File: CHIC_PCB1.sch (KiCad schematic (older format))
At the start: 39 parts, among them J1 Conn_01x06_Female, P1 USB_C_Plug_USB2.0, SW1 SW_Push, U1 ATmega328P-MMH, U2 MCP73831-2-OT, U3 ESP-12E, U4 AT42QT1010-M

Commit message: Second version finished, to be verified
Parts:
- removed C7: 0.1u, Capacitor_SMD:C_0805_2012Metric, symbol Device:C
- removed C8: C, Capacitor_SMD:C_0805_2012Metric, symbol Device:C
- removed J1: Conn_01x06_Female, Connector_Harwin:Harwin_M20-89006xx_1x06_P2.54mm_Horizontal, symbol Connector:Conn_01x06_Female
- removed TP1, TP2, TP3: TestPoint, Connector_PinHeader_1.00mm:PinHeader_1x01_P1.00mm_Horizontal, symbol Connector:TestPoint
- removed U1: ATmega328P-MMH, Package_DFN_QFN:QFN-28-1EP_4x4mm_P0.45mm_EP2.4x2.4mm, symbol MCU_Microchip_ATmega:ATmega328P-MMH
- added D3: LED, symbol Device:LED
- added D4, D5: D_Schottky, symbol Device:D_Schottky
- added J1: FTDI or UART cable, symbol Connector_Generic:Conn_01x06
- added R11: 10k, symbol Device:R
- added SW2: SW_Push, symbol Switch:SW_Push
- added U1: AP2112K-3.3, Package_TO_SOT_SMD:SOT-23-5, symbol Regulator_Linear:AP2112K-3.3
- C3: value 100n -> 10u; footprint Capacitor_SMD:C_0805_2012Metric -> (none)
- R5, R9: footprint Resistor_SMD:R_0603_1608Metric -> (none)
- R6: value 10k -> 2k; footprint Resistor_SMD:R_0603_1608Metric -> (none)
- R7: value R -> 10k; footprint Resistor_SMD:R_0603_1608Metric -> (none)
- SW1: footprint Button_Switch_SMD:SW_Push_1P1T_NO_CK_KSC7xxJ -> (none)
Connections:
- net labels added: ADC, CH_PD, GPIO0, GPIO2, RXD, TXD, Vbat, Vin, nRESET
- net labels removed: MC_RX, MC_TX, VCC, Vtouch, cts, rst, ucc
- wire segments 109 -> 87
- no-connect marks 0 -> 1
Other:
- note added: "3.3V out, 500mA regulator to combine the battery input and the UART cable input.\nTherefore, it's not a problem to use 5v instead of 3.3v for the UART cable"
- note added: "Battery Charger with USB-C connection"
- note added: "CHIC Sensor Module"
- note added: "ESP8266 Module\nActs as the MC of the boad to read the sensor value and send it to host server."
- note added: "Reboot mode: "If GPIO0 is held low during power-up, it starts boot-mode".\nGPIO2 can also be used for boatload, so keep it high.\n"
- note added: "Touch Sensor Module (hopefully we can create our own soon)"
- note added: "UART Cable to flash the ESP8266, and for debuging. \nESP8266 can be flashed easily with Atom's Platform IO software."
- note removed: "Battery Charger and USB-C connection"
- note removed: "ESP8266 Wifi Module"
- note removed: "Microcontrolleur ATMega \n"
- note removed: "Touch Sensor Module"
- moved on the sheet: BatteryConnector1, C1, C2, C4, C5, C6, D1, D2, Electrode1, H1, H3, H4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

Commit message: Test de github
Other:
- note added: "fgdhgfd"
- note added: "test"
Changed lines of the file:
@@
 5v
 NoConn ~ 6950 3450
+Text Notes 450  -300 0    50   ~ 0
+test
+Text Notes 1050 -150 0    50   ~ 0
+fgdhgfd
 $EndSCHEMATC

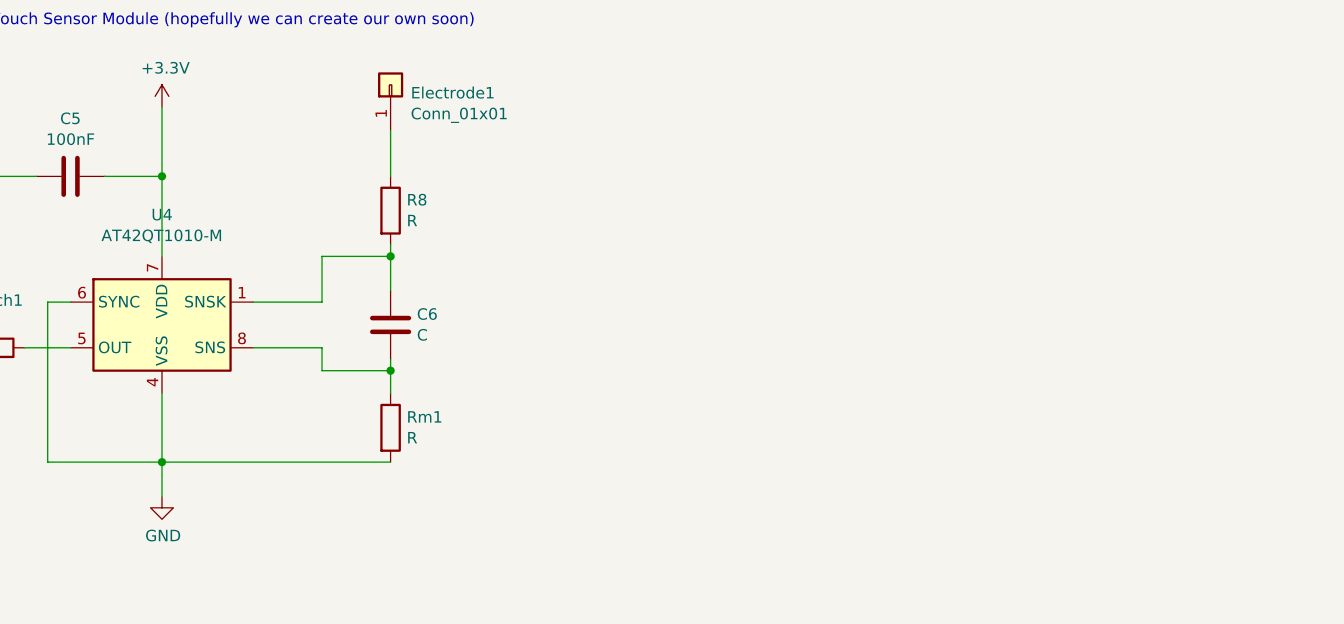
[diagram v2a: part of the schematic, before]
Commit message: Corrected touch sensor circuit. Added capacitor value.
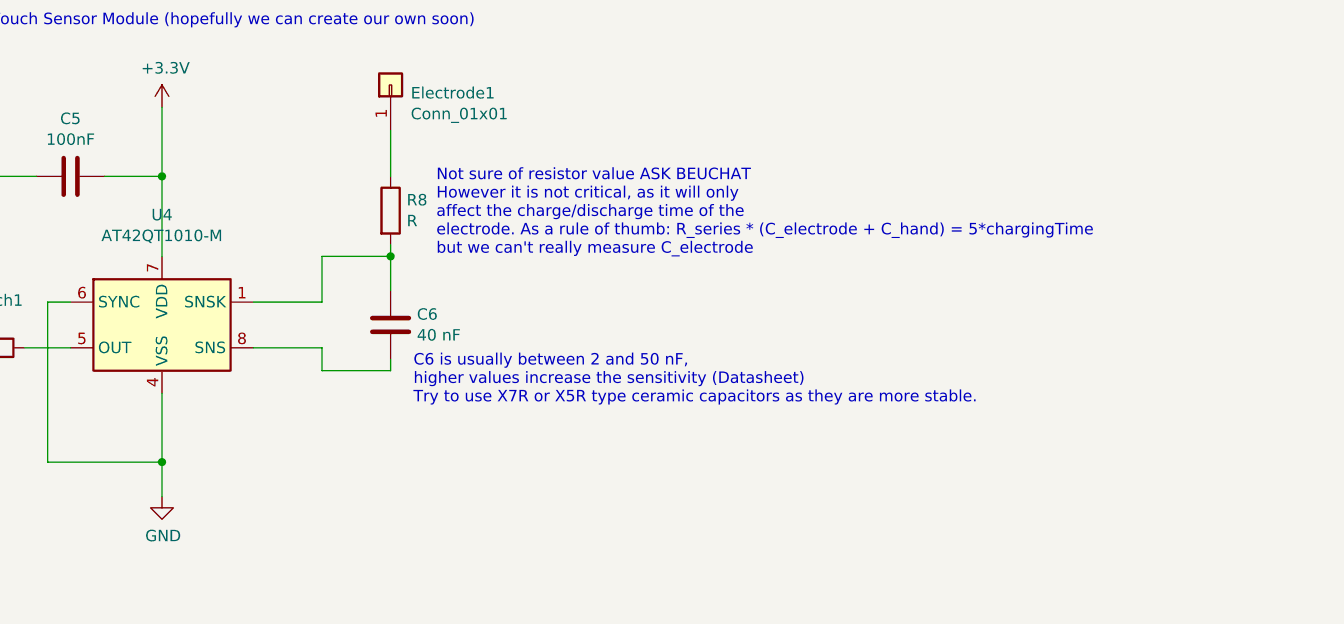
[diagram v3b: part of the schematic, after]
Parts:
- removed Rm1: R, Resistor_SMD:R_0603_1608Metric, symbol Device:R
- C6: value C -> 40 nF
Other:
- note added: "C6 is usually between 2 and 50 nF, \nhigher values increase the sensitivity (Datasheet)\nTry to use X7R or X5R type ceramic capacitors as they are more stable."
- note added: "Not sure of resistor value ASK BEUCHAT\nHowever it is not critical, as it will only \naffect the charge/discharge time of the \nelectrode. As a rule of thumb: R_series * (C_electrode + C_hand) = 5*chargingTime\nbut we can't really measure C_electrode"
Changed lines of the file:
@@
 P 9900 5450
 F 0 "C6" H 10015 5496 50  0000 L CNN
-F 1 "C" H 10015 5405 50  0000 L CNN
+F 1 "40 nF" H 10015 5405 50  0000 L CNN
 F 2 "Capacitor_SMD:C_0805_2012Metric" H 9938 5300 50  0001 C CNN
 F 3 "~" H 9900 5450 50  0001 C CNN
 	1    9900 5450
-	1    0    0    -1
-$EndComp
-$Comp
-L Device:R Rm1
-U 1 1 5EA16CDE
-P 9900 5900
-F 0 "Rm1" H 9970 5946 50  0000 L CNN
-F 1 "R" H 9970 5855 50  0000 L CNN
-F 2 "Resistor_SMD:R_0603_1608Metric" V 9830 5900 50  0001 C CNN
-F 3 "~" H 9900 5900 50  0001 C CNN
-	1    9900 5900
 	1    0    0    -1
 $EndComp
@@
 Wire Wire Line
 	8900 5750 8900 6050
-Wire Wire Line
-	8900 6050 9900 6050
 Connection ~ 8900 6050
 Wire Wire Line
 	8900 6050 8900 6200
-Wire Wire Line
-	9900 5750 9900 5650
 Wire Wire Line
 	9900 5300 9900 5150
@@
 Wire Wire Line
 	9600 5650 9900 5650
-Connection ~ 9900 5650
 Wire Wire Line
 	9900 5650 9900 5600
@@
 Text Notes 1050 -150 0    50   ~ 0
 fgdhgfd
+Text Notes 10000 5800 0    50   ~ 0
+C6 is usually between 2 and 50 nF, \nhigher values increase the sensitivity (Datasheet)\nTry to use X7R or X5R type ceramic capacitors as they are more stable.
+Text Notes 10100 5150 0    50   ~ 0
+Not sure of resistor value ASK BEUCHAT\nHowever it is not critical, as it will only \naffect the charge/discharge time of the \nelectrode. As a rule of thumb: R_series * (C_electrode + C_hand) = 5*chargingTime\nbut we can't really measure C_electrode
 $EndSCHEMATC
